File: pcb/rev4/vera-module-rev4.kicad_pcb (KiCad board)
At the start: 2 copper layers, 96.5 x 55 mm, 108 parts, among them J1 Bus, J2 Prog, J3 SD_Card, J4 Composite, J5 VGA, J9 S-video, U1 ICE40UP5K-SG48ITR50, U10 MIC5504-3.3YM5, U11 THS7314D, U2 74AHC00PW, U3 SN74CBTD3861PWR, U4 74CBTLV3126PW,118, U5 74LVC4245APW, U6 WM8524CGEDT, U7 W25Q16JVSNIQ, U9 AP3417CKTR-G1, X1 SG5032CAN_25.000000M-TJGA3

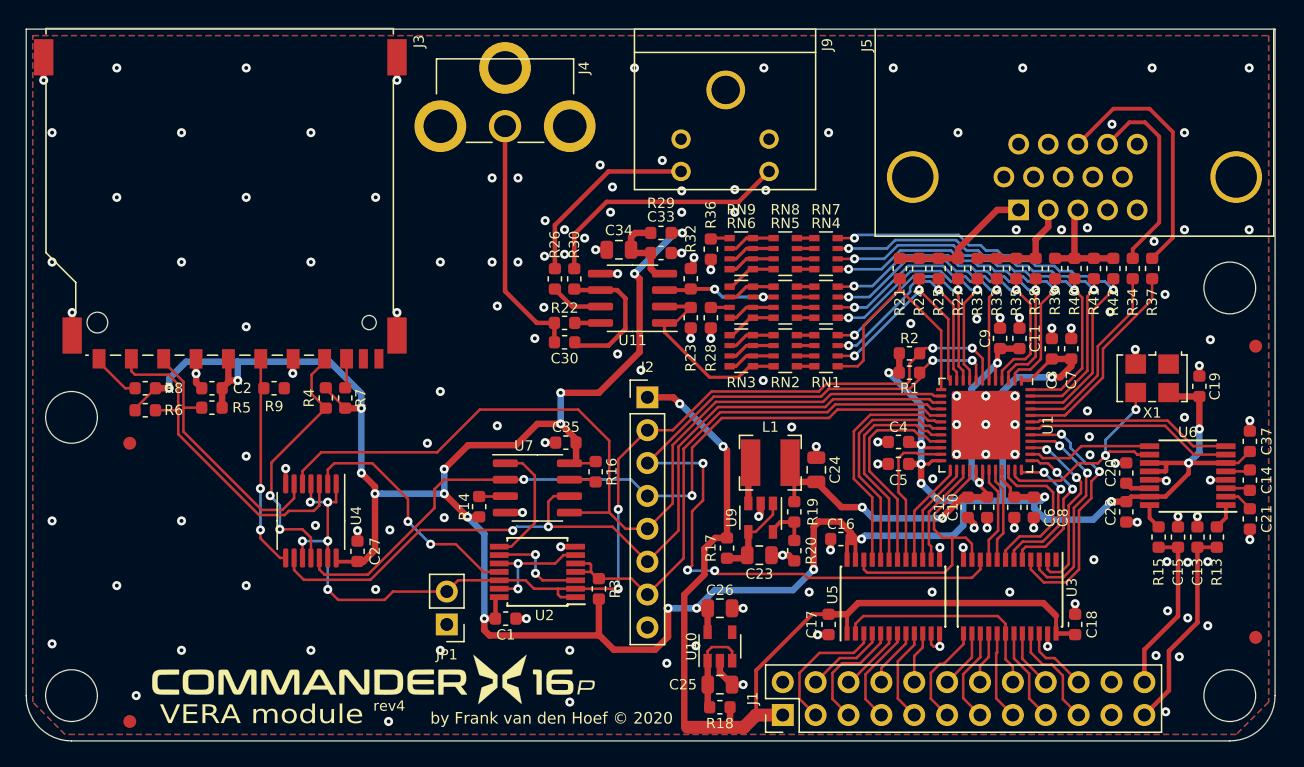
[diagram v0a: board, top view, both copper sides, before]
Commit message: Update with new footprints
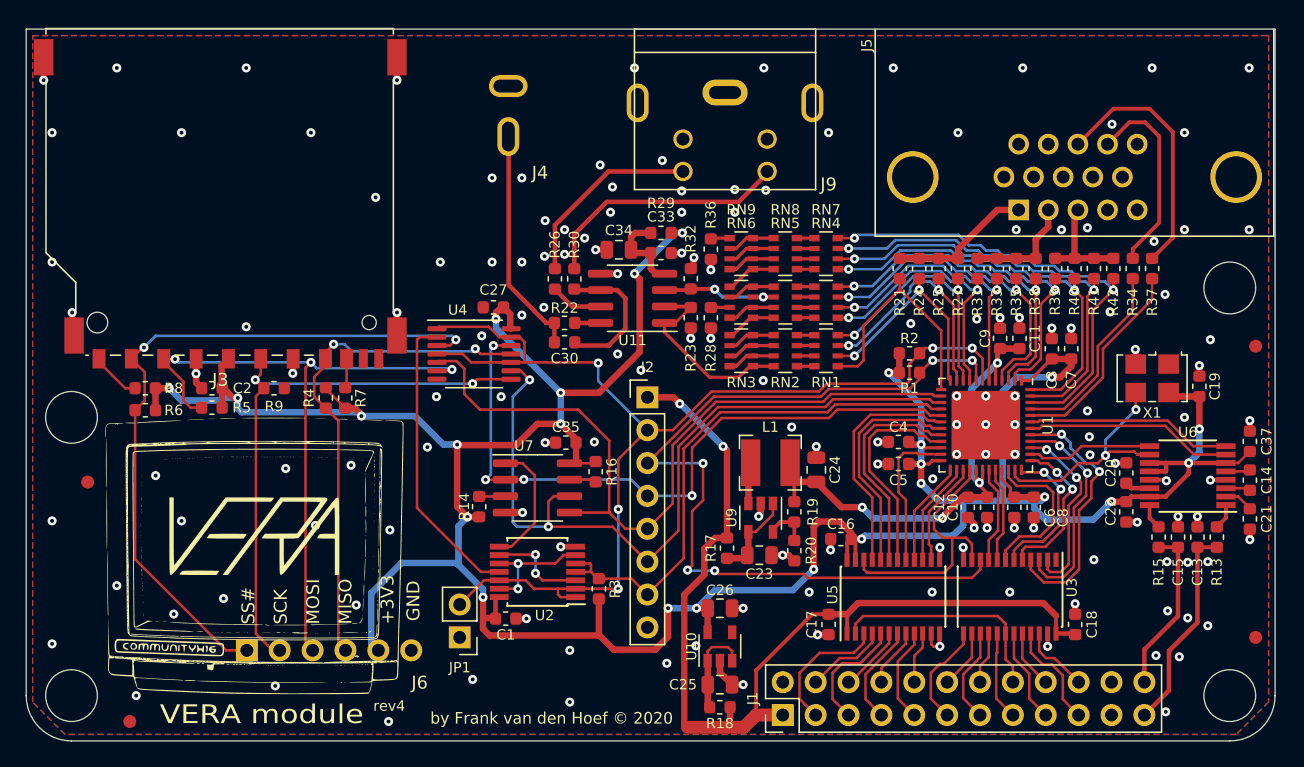
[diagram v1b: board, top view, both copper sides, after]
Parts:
- added J6: Conn_01x06_Pin, Connector_PinHeader_2.54mm:PinHeader_1x06_P2.54mm_Vertical, F.Cu at (118.5, 128.0)
- J3: footprint Connector_Card:SD_TE_2041021 -> vera-module:SD-102
- J4: footprint vera-module:RCJ-014 -> vera-module:AV-5
- J9: footprint vera-module:MD-40S -> vera-module:MDC-4-02
- LOGO1: footprint vera-module:x16plogo -> vera-module:VERA_CE_Logo2
- moved C27 21.6 mm to (137.6, 101.5), turned to 180 degrees
- moved U4 18.0 mm to (136.1, 105.1), turned to 0 degrees
- moved LOGO1 13.4 mm to (119.1, 120.5)
- moved FID3 4.42 mm to (106.2, 115.0)
- moved J4 3.01 mm to (138.8, 80.0), turned to 180 degrees
- moved JP1 1.41 mm to (135.0, 127.0)
- turned R6 to 180 degrees
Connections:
- net Net-(J3-Pad1) renamed /SKT_SSEL_N
- net Net-(J3-Pad2) renamed /SKT_MOSI
- net Net-(J3-Pad5) renamed /SKT_SCK
- net Net-(J3-Pad7) renamed /SKT_MISO
- J3 pad 10: Net-(J3-Pad10) -> unconnected-(J3-CARD_DETECT-Pad10)
- J3 pad 11: Net-(J3-Pad11) -> unconnected-(J3-WRITE_PROTECT-Pad11)
- J5 pad 11: Net-(J5-Pad11) -> unconnected-(J5-Pad11)
- J5 pad 12: Net-(J5-Pad12) -> unconnected-(J5-Pad12)
- J5 pad 15: Net-(J5-Pad15) -> unconnected-(J5-Pad15)
- J5 pad 4: Net-(J5-Pad4) -> unconnected-(J5-Pad4)
- J5 pad 9: Net-(J5-Pad9) -> unconnected-(J5-Pad9)
- U10 pad 4: Net-(U10-Pad4) -> unconnected-(U10-NC-Pad4)
- X1 pad 1: Net-(X1-Pad1) -> unconnected-(X1-~{ST}-Pad1)
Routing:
- net /SKT_MOSI: track 20.2 -> 51.5 mm, vias 0 -> 3
- net /SKT_SSEL_N: track 26.1 -> 54.8 mm, vias 0 -> 2
- net /SKT_SCK: track 16.5 -> 43.5 mm
- net /SKT_MISO: track 20.4 -> 38.1 mm
- net SPI_MOSI: track 69.5 -> 58.7 mm
- net +3V3: track 249.8 -> 256.3 mm, vias 26 -> 24
- net SPI_SCK: track 67.0 -> 60.5 mm
- net SPI_MISO: track 58.6 -> 52.8 mm, vias 2 -> 4
- net SD_SSEL_N: track 19.0 -> 23.0 mm, vias 2 -> 0
- net +1V2: track 39.6 -> 37.0 mm
- net GND: track 56.8 -> 54.8 mm, vias 159 -> 155
- net FPGA_CDONE: track 86.3 -> 88.1 mm, vias 9 -> 5
- net Net-(J4-In): track 19.1 -> 17.7 mm
- net Net-(RN2-R1.2): track 15.5 -> 14.3 mm
- net VGA_R0: track 20.4 -> 19.6 mm
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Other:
- net class Default removed
- board text added: "+3V3"
- board text added: "GND"
- board text added: "MISO"
- board text added: "MOSI"
- board text added: "SCK"
- board text added: "SS#"

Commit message: ESD protection and HDMI headers
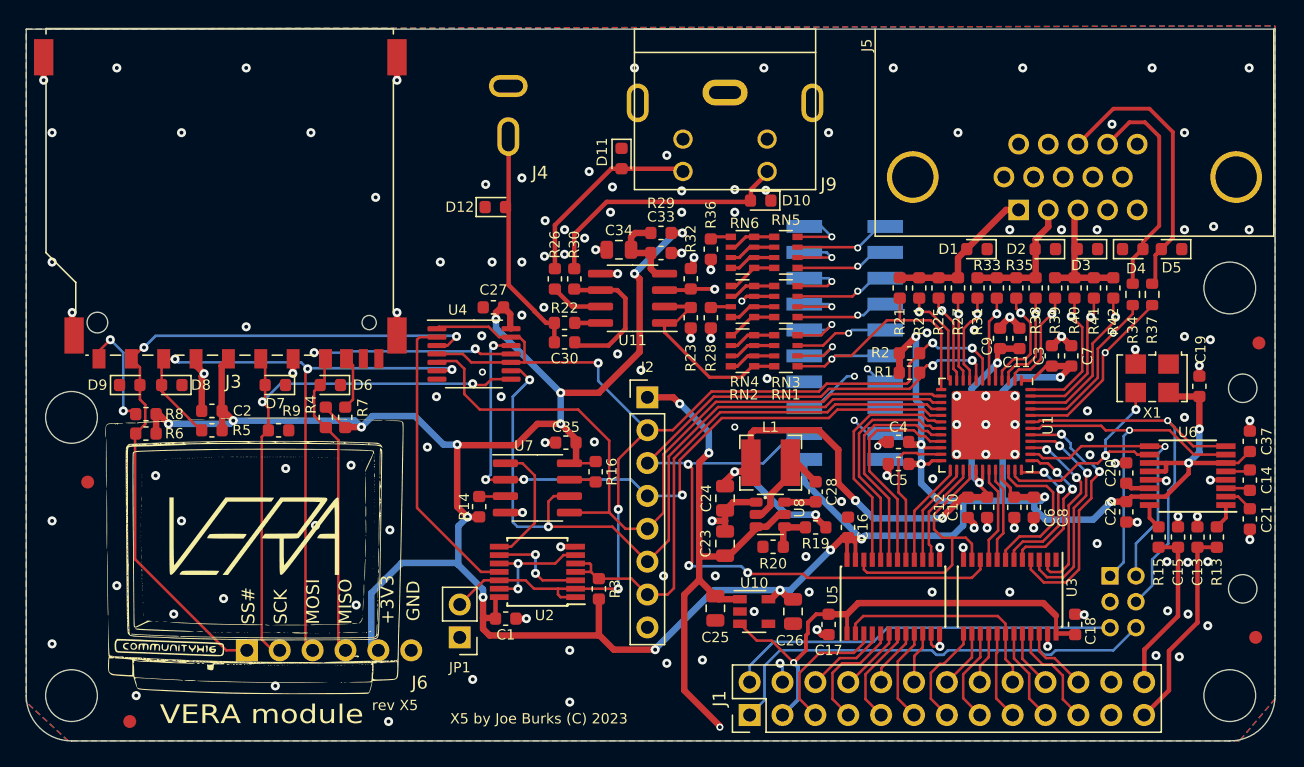
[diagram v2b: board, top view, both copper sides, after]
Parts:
- removed R17, R18: 1, Resistor_SMD:R_0603_1608Metric
- removed RN7, RN8, RN9: CAY16-1001F4LF, Resistor_SMD:R_Array_Convex_4x0603
- removed U9: AP3417CKTR-G1, Package_TO_SOT_SMD:SOT-23-5
- added C28: 100nF, Capacitor_SMD:C_0603_1608Metric, F.Cu at (162.5, 115.8)
- added D1: D_TVS_Filled, Diode_SMD:D_0603_1608Metric, F.Cu at (175.0, 97.0)
- added D10: D_TVS_Filled, Diode_SMD:D_0603_1608Metric, F.Cu at (158.2, 93.2)
- added D11: D_TVS_Filled, Diode_SMD:D_0603_1608Metric, F.Cu at (147.5, 90.0)
- added D12: D_TVS_Filled, Diode_SMD:D_0603_1608Metric, F.Cu at (137.8, 93.8)
- added D2: D_TVS_Filled, Diode_SMD:D_0603_1608Metric, F.Cu at (180.2, 97.0)
- added D3: D_TVS_Filled, Diode_SMD:D_0603_1608Metric, F.Cu at (183.5, 97.0)
- added D4: D_TVS_Filled, Diode_SMD:D_0603_1608Metric, F.Cu at (187.0, 97.0)
- added D5: D_TVS_Filled, Diode_SMD:D_0603_1608Metric, F.Cu at (190.0, 97.0)
- added D6: D_TVS_Filled, Diode_SMD:D_0603_1608Metric, F.Cu at (125.0, 107.5)
- added D7: D_TVS_Filled, Diode_SMD:D_0603_1608Metric, F.Cu at (120.8, 107.5)
- added D8: D_TVS_Filled, Diode_SMD:D_0603_1608Metric, F.Cu at (112.8, 107.5)
- added D9: D_TVS_Filled, Diode_SMD:D_0603_1608Metric, F.Cu at (109.5, 107.5)
- added H5: MountingHole, MountingHole:MountingHole_2.2mm_M2, F.Cu at (195.5, 123.2)
- added H6: MountingHole, MountingHole:MountingHole_2.2mm_M2, F.Cu at (195.5, 107.8)
- added J7: HDMI Video Exp., Connector_PinSocket_2.00mm:PinSocket_2x10_P2.00mm_Vertical_SMD, B.Cu at (164.8, 104.2)
- added J8: I2X, Connector_PinSocket_2.00mm:PinSocket_2x03_P2.00mm_Vertical, B.Cu at (185.2, 122.2)
- added U8: AP62200WU-7, vera-module:TSOT26-6, F.Cu at (159.0, 117.5)
- J1: footprint Connector_PinHeader_2.54mm:PinHeader_2x12_P2.54mm_Vertical -> Connector_PinHeader_2.54mm:PinHeader_2x13_P2.54mm_Vertical
- R19: value 47k -> 5K76
- R20: value 47k -> 10K
- RN1, RN3, RN5: value CAY16-1001F4LF -> CAY16-2001F4LF
- moved C24 7.39 mm to (155.5, 116.2), turned to -90 degrees
- moved RN4 6.45 mm to (156.8, 101.0)
- moved C25 5.91 mm to (154.8, 124.8), turned to -90 degrees
- moved C26 5.66 mm to (160.8, 125.0), turned to -90 degrees
- moved RN3 5.13 mm to (160.2, 101.0)
- moved RN6 3.85 mm to (156.8, 97.2)
- moved RN5 3.85 mm to (160.2, 97.2)
- moved U10 3.78 mm to (157.8, 125.0), turned to 0 degrees
- moved RN2 3.30 mm to (156.8, 104.8)
- moved R9 3.27 mm to (121.0, 111.0)
- moved RN1 3.10 mm to (160.2, 104.8)
- moved C23 2.80 mm to (155.5, 119.8), turned to 90 degrees
- moved J1 2.56 mm to (157.4, 133.0)
- moved R19 2.04 mm to (162.5, 118.5), turned to 180 degrees
- moved R8 2.00 mm to (110.8, 109.8)
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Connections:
- net Net-(J5-Pad1) renamed /VGA_ANL_R
- net Net-(J5-Pad13) renamed /VGA_HSYNC_OUT
- net Net-(J5-Pad14) renamed /VGA_VSYNC_OUT
- net Net-(J5-Pad2) renamed /VGA_ANL_G
- net Net-(J5-Pad3) renamed /VGA_ANL_B
- C23 pad 1: Net-(U9-EN) -> +5V
- C25 pad 1: Net-(U10-EN) -> +5V
- J1 pad 1: +5V -> SCL
- J1 pad 10: BUS_D0_5V -> BUS_D2_5V
- J1 pad 11: BUS_CS#_5V -> BUS_D1_5V
- J1 pad 12: BUS_RES#_5V -> BUS_D0_5V
- J1 pad 13: BUS_WR#_5V -> BUS_CS#_5V
- J1 pad 14: BUS_IRQ#_5V -> BUS_RES#_5V
- J1 pad 15: BUS_A4_5V -> BUS_WR#_5V
- J1 pad 16: BUS_RD#_5V -> BUS_IRQ#_5V
- J1 pad 17: BUS_A2_5V -> BUS_A4_5V
- J1 pad 18: BUS_A3_5V -> BUS_RD#_5V
- J1 pad 19: BUS_A0_5V -> BUS_A2_5V
- J1 pad 2: GND -> SDA
- J1 pad 20: BUS_A1_5V -> BUS_A3_5V
- J1 pad 21: GND -> BUS_A0_5V
- J1 pad 22: GND -> BUS_A1_5V
- J1 pad 23: L_AUDIO -> GND
- J1 pad 24: R_AUDIO -> GND
- J1 pad 3: BUS_D7_5V -> +5V
- J1 pad 4: BUS_D6_5V -> GND
- J1 pad 5: BUS_D5_5V -> BUS_D7_5V
- J1 pad 6: BUS_D4_5V -> BUS_D6_5V
- J1 pad 7: BUS_D3_5V -> BUS_D5_5V
- J1 pad 8: BUS_D2_5V -> BUS_D4_5V
- J1 pad 9: BUS_D1_5V -> BUS_D3_5V
- R23 pad 1: Net-(RN2-R1.2) -> Net-(RN1-R1.2)
- R28 pad 2: Net-(RN6-R2.2) -> Net-(RN4-R2.2)
- R32 pad 1: Net-(RN5-R3.2) -> Net-(RN3-R3.2)
- R36 pad 2: Net-(RN9-R4.2) -> Net-(RN6-R4.2)
- RN2 pad 6: Net-(RN2-R3.2) -> Net-(RN1-R4.2)
- RN2 pad 7: Net-(RN2-R2.2) -> Net-(RN1-R3.2)
- RN2 pad 8: Net-(RN2-R1.2) -> Net-(RN1-R2.2)
- RN3 pad 1: Net-(RN2-R1.2) -> VGA_G3
- RN3 pad 2: Net-(RN2-R2.2) -> VGA_G2
- RN3 pad 3: Net-(RN2-R3.2) -> VGA_G1
- RN3 pad 4: Net-(RN2-R4.2) -> VGA_G0
- RN3 pad 6: Net-(RN2-R4.2) -> Net-(RN3-R3.2)
- RN3 pad 7: Net-(RN2-R3.2) -> Net-(RN3-R2.2)
- RN3 pad 8: Net-(RN2-R2.2) -> Net-(RN2-R4.2)
- RN4 pad 1: VGA_G3 -> Net-(RN2-R4.2)
- RN4 pad 2: VGA_G2 -> Net-(RN3-R2.2)
- RN4 pad 3: VGA_G1 -> Net-(RN3-R3.2)
- RN4 pad 4: VGA_G0 -> Net-(RN3-R4.2)
- RN4 pad 6: Net-(RN4-R3.2) -> Net-(RN3-R4.2)
- RN4 pad 8: Net-(RN4-R1.2) -> Net-(RN3-R2.2)
- RN5 pad 1: Net-(RN4-R1.2) -> VGA_B3
- RN5 pad 2: Net-(RN4-R2.2) -> VGA_B2
- RN5 pad 3: Net-(RN4-R3.2) -> VGA_B1
- RN5 pad 4: Net-(RN4-R4.2) -> VGA_B0
- RN5 pad 8: Net-(RN3-R4.2) -> Net-(RN4-R4.2)
- RN6 pad 1: Net-(RN3-R4.2) -> Net-(RN4-R4.2)
- RN6 pad 7: Net-(RN6-R2.2) -> Net-(RN5-R3.2)
- U10 pad 1: Net-(U10-EN) -> +5V
- U10 pad 3: Net-(U10-EN) -> +5V
- U11 pad 1: Net-(RN2-R1.2) -> Net-(RN1-R1.2)
- U11 pad 2: Net-(RN2-R1.2) -> Net-(RN1-R1.2)
- U11 pad 3: Net-(RN5-R3.2) -> Net-(RN3-R3.2)
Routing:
- net SCL: track 0.00 -> 34.8 mm
- net SDA: track 0.00 -> 30.3 mm
- net SYSCLK: track 17.9 -> 43.3 mm, vias 2 -> 3
- net VGA_HSYNC: track 16.0 -> 38.7 mm, vias 0 -> 2
- net VGA_VSYNC: track 14.9 -> 35.3 mm, vias 0 -> 2
- net +1V2: track 37.0 -> 55.0 mm, vias 4 -> 6
- net AUDIO_LRCK: track 16.0 -> 31.4 mm, vias 0 -> 1
- net Net-(RN2-R1.2): track 14.3 -> 0.00 mm
- net Net-(RN1-R1.2): track 1.35 -> 14.5 mm
- net AUDIO_BCK: track 9.71 -> 21.8 mm, vias 0 -> 1
- net +5V: track 73.9 -> 85.9 mm, vias 2 -> 4
- net AUDIO_DATA: track 16.1 -> 28.0 mm, vias 0 -> 1
- net Net-(RN3-R3.2): track 0.00 -> 9.52 mm, vias 0 -> 2
- net FPGA_CRESET_B: track 67.3 -> 74.6 mm
- net Net-(U10-EN): track 7.06 -> 0.00 mm
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- added copper zone on In1.Cu, net GND
- added copper zone on In2.Cu, net GND
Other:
- copper layers 2 -> 4
- board text added: "ADAT"
- board text added: "B0"
- board text added: "B1"
- board text added: "B2"
- board text added: "B3"
- board text added: "BCK"
- board text added: "G0"
- board text added: "G1"
- board text added: "G2"
- board text added: "G3"
- board text added: "HS"
- board text added: "LRCK"
- board text added: "NC"
- board text added: "PCLK"
- board text added: "R0"
- board text added: "R1"
- board text added: "R2"
- board text added: "R3"
- board text added: "RST"
- board text added: "SCL"
- board text added: "SDA"
- board text added: "VS"
- board text added: "X5 by Joe Burks (C) 2023"
- board text added: "rev X5"
- board text removed: "rev4"
